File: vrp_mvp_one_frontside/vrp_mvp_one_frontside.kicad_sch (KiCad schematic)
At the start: 23 parts, among them J1 Micro_SD_Card, J2 BACKSIDE_INTERFACE_1, J3 VIB_OUT, J4 USB_C_Receptacle_USB2.0_16P, J6 DEBUG, J7 BACKSIDE_INTERFACE_2, Q1 MMBT2222A, Q2 MMBT2222A, U2 NHD-C0220BIZ

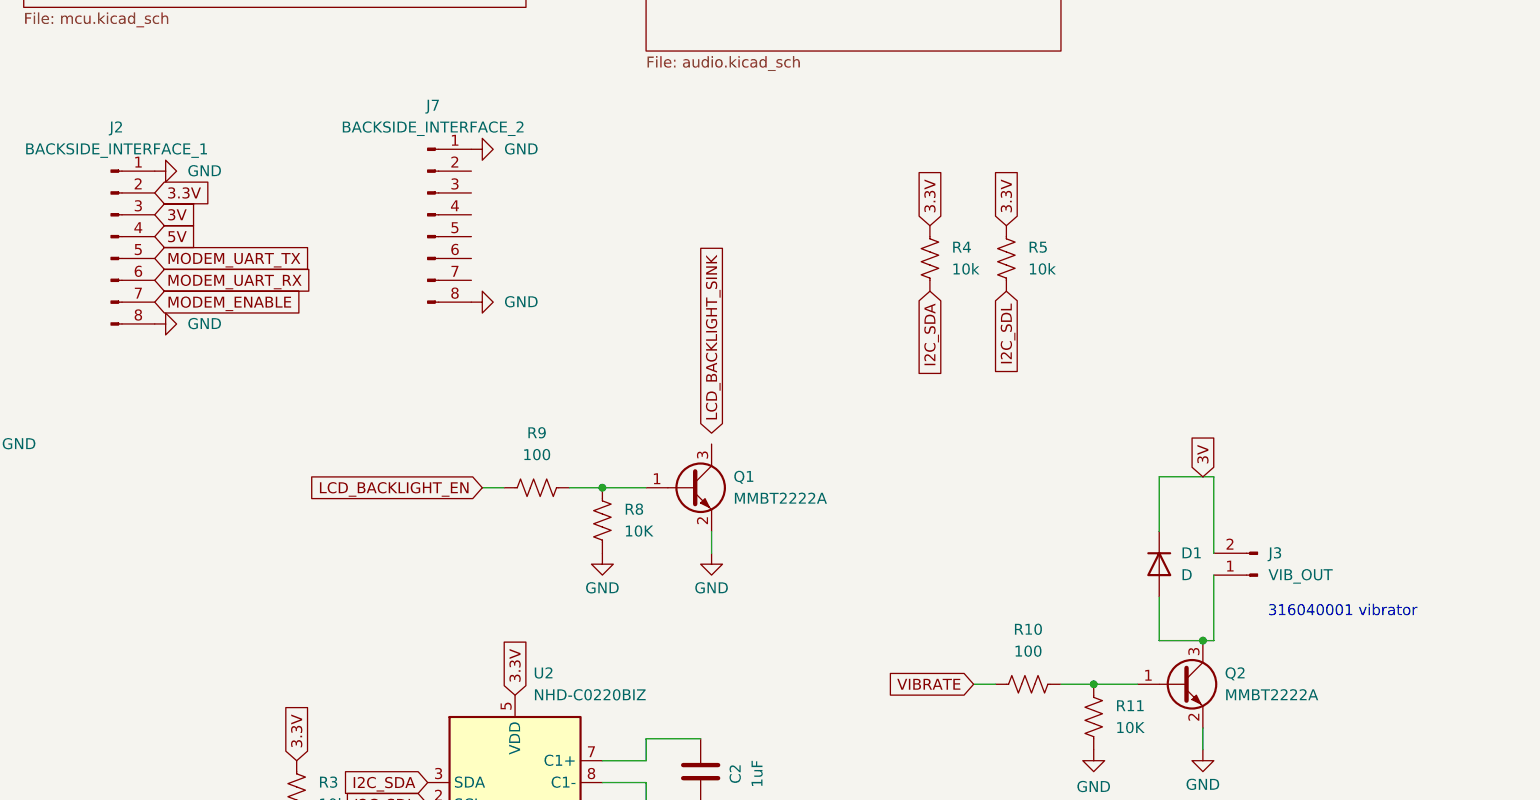
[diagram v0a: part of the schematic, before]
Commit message: audio, more routing, switched to lipo battery
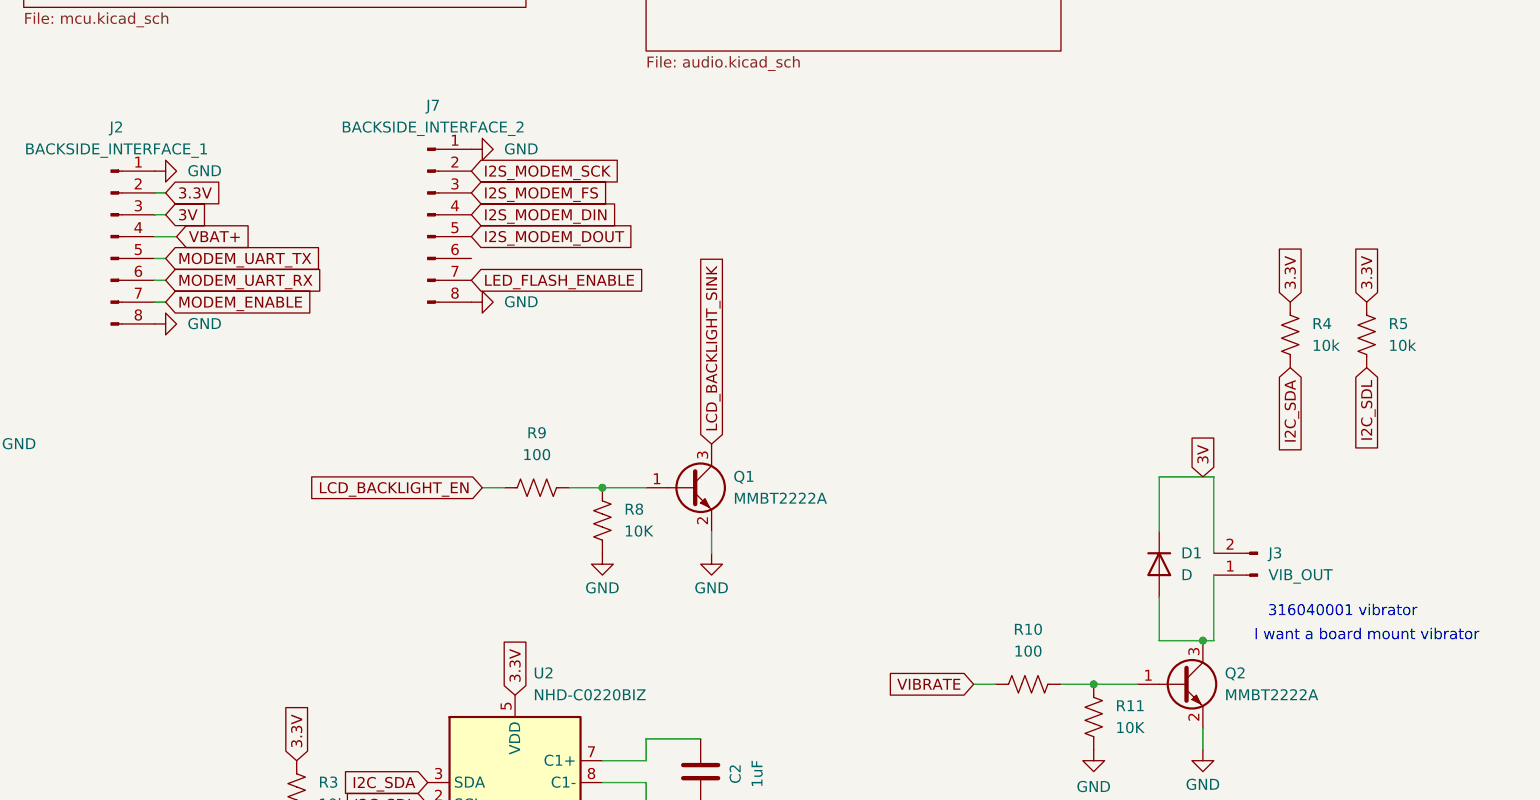
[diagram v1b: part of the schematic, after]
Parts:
- R8, R9: footprint Resistor_SMD:R_1206_3216Metric_Pad1.30x1.75mm_HandSolder -> Resistor_SMD:R_0805_2012Metric_Pad1.20x1.40mm_HandSolder
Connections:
- net LCD_BACKLIGHT_SINK: now also Q1.3 (C)
- net I2S_MODEM_SCK: now reaches J7.2 (Pin_2)
- net I2S_MODEM_FS: now reaches J7.3 (Pin_3)
- net I2S_MODEM_DIN: now reaches J7.4 (Pin_4)
- net I2S_MODEM_DOUT: now reaches J7.5 (Pin_5)
- net LED_FLASH_ENABLE: now reaches J7.7 (Pin_7)
- net 5V renamed VBAT+
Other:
- note added: "I want a board mount vibrator"
- moved on the sheet: R4, R5

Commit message: changes
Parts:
- removed D1: D, symbol Device:D
- removed J3: VIB_OUT, Connector_PinHeader_2.54mm:PinHeader_1x02_P2.54mm_Vertical, symbol Connector:Conn_01x02_Pin
- removed Q1, Q2: MMBT2222A, Package_TO_SOT_SMD:SOT-23_Handsoldering, symbol Transistor_BJT:MMBT2222A
- removed R10, R9: 100, Resistor_SMD:R_0805_2012Metric_Pad1.20x1.40mm_HandSolder, symbol Device:R_US
- removed R11, R8: 10K, Resistor_SMD:R_0805_2012Metric_Pad1.20x1.40mm_HandSolder, symbol Device:R_US
- added R15, R7: 10k, Resistor_SMD:R_0805_2012Metric_Pad1.20x1.40mm_HandSolder, symbol Device:R_US
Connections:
- net GND: now also R15.2
- net I2S_MODEM_DOUT: now also J7.3 (Pin_3); no longer J7.5 (Pin_5)
- net I2S_MODEM_FS: now also J7.5 (Pin_5); no longer J7.3 (Pin_3)
- net MODEM_UART_RX: now also J2.5 (Pin_5); no longer J2.6 (Pin_6)
- net MODEM_UART_TX: now also J2.6 (Pin_6); no longer J2.5 (Pin_5)
- net VBAT+: now also R7.1
- net CHARGE_STATUS: now reaches J7.6 (Pin_6)
- net I2C_SDL renamed I2C_SCL
- new net BATT_SENSE: R15.1, R7.2
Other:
- added sheet switching (switching.kicad_sch)
- note removed: "316040001 vibrator"
- note removed: "I want a board mount vibrator"
- moved on the sheet: C1, C2, J6, R3, U2

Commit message: removed vibration motor circuitry
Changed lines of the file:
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@@
-	(wire
-		(pts
-			(xy 243.84 109.22) (xy 250.19 109.22)
-		)
-		(stroke
-			(width 0)
-			(type default)
-		)
-	)
 	(wire
 		(pts
